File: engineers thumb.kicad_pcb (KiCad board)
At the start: 2 copper layers, 71.1 x 63.5 mm, 53 parts, among them J1 INPUT, J2 9V, J3 GND, J4 Out, J5 GND, J6 LED+, Q1 Q_PMOS_GSD, Q2 BC327, SW1 TREBLE_BOOST, U1 TL072, U2 TL072, U3 LM13700

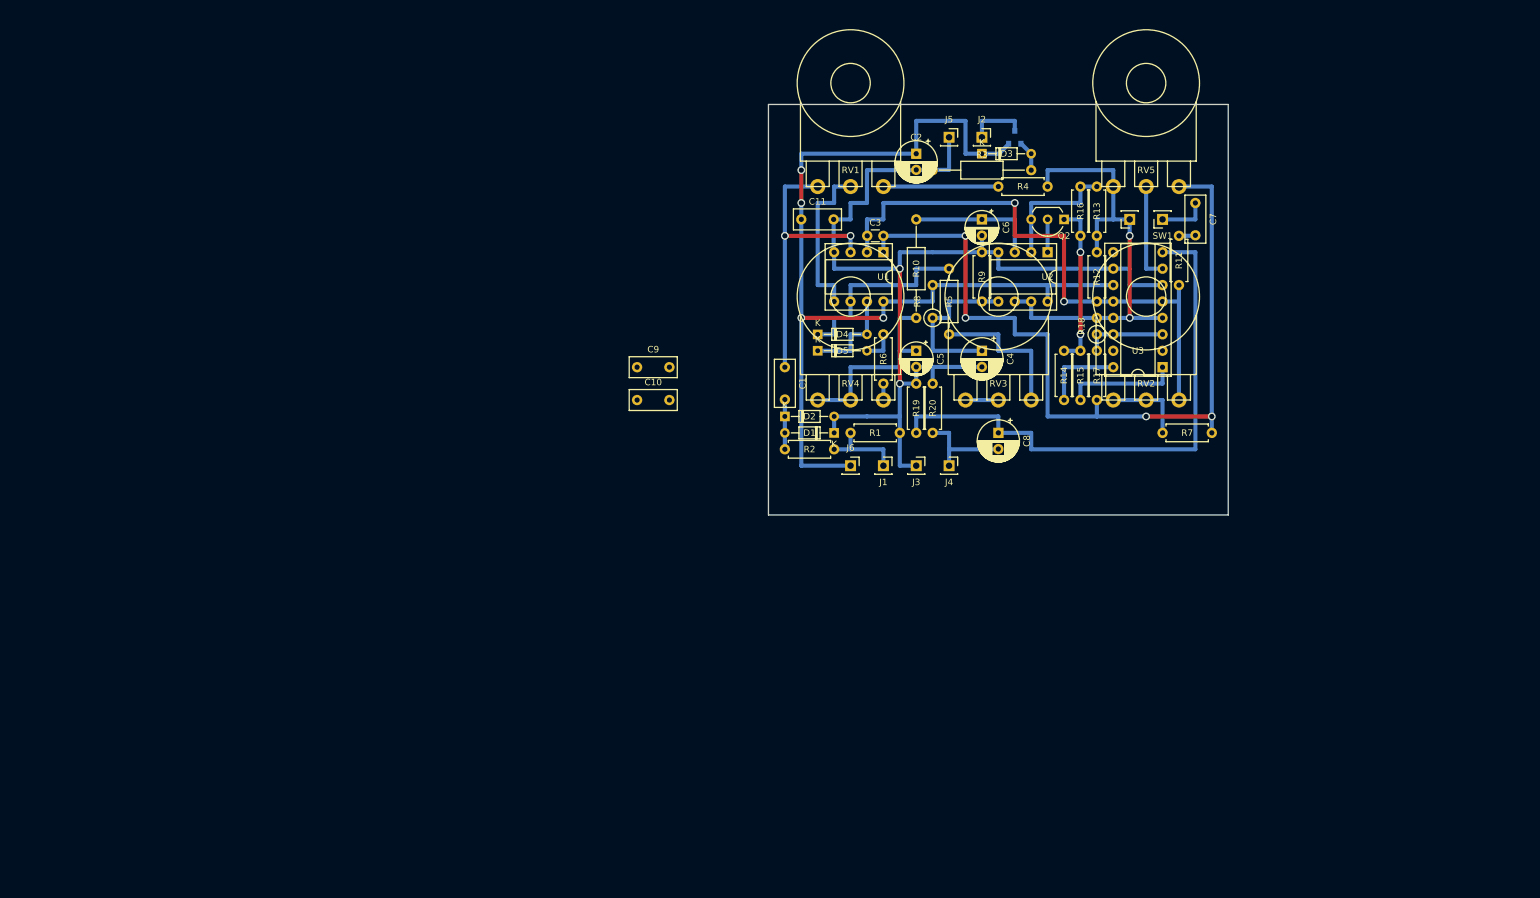
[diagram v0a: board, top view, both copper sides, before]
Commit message: Corrected footprints
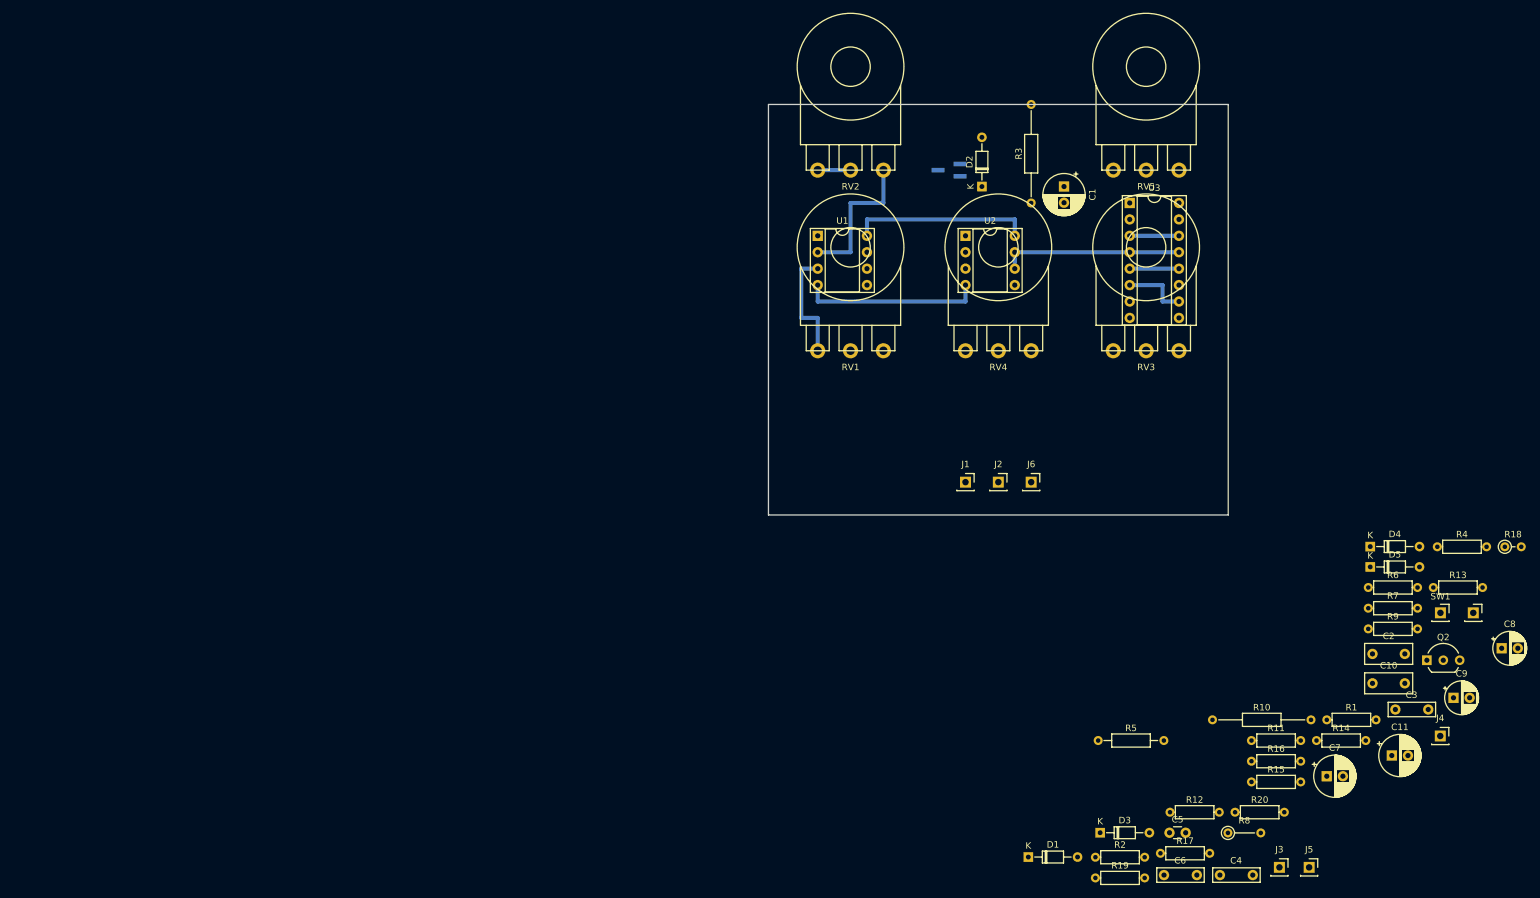
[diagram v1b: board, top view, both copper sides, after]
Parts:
- C1: value 10n -> 47u; footprint Capacitor_THT:C_Rect_L7.2mm_W3.0mm_P5.00mm_FKS2_FKP2_MKS2_MKP2 -> Capacitor_THT:CP_Radial_D6.3mm_P2.50mm
- C10: value 100n -> 4.7n-10n
- C11: value 100n -> 10u; footprint Capacitor_THT:C_Rect_L7.2mm_W3.0mm_P5.00mm_FKS2_FKP2_MKS2_MKP2 -> Capacitor_THT:CP_Radial_D6.3mm_P2.50mm
- C2: value 47u -> 10n; footprint Capacitor_THT:CP_Radial_D6.3mm_P2.50mm -> Capacitor_THT:C_Rect_L7.2mm_W3.0mm_P5.00mm_FKS2_FKP2_MKS2_MKP2
- C3: value 100p -> 100n; footprint Capacitor_THT:C_Disc_D3.0mm_W1.6mm_P2.50mm -> 2.Breadboard components:C_Box_P5.08mm
- C4: value 10u -> 100n; footprint Capacitor_THT:CP_Radial_D6.3mm_P2.50mm -> 2.Breadboard components:C_Box_P5.08mm
- C5: value 1u-2u2 -> 100p; footprint Capacitor_THT:CP_Radial_D5.0mm_P2.50mm -> Capacitor_THT:C_Disc_D3.0mm_W1.6mm_P2.50mm
- C6: value 1u-2u2 -> 100n; footprint Capacitor_THT:CP_Radial_D5.0mm_P2.50mm -> 2.Breadboard components:C_Box_P5.08mm
- C7: value 4.7n-10n -> 10u; footprint Capacitor_THT:C_Rect_L7.2mm_W3.0mm_P5.00mm_FKS2_FKP2_MKS2_MKP2 -> Capacitor_THT:CP_Radial_D6.3mm_P2.50mm
- C8: value 10u -> 1u-2u2; footprint Capacitor_THT:CP_Radial_D6.3mm_P2.50mm -> Capacitor_THT:CP_Radial_D5.0mm_P2.50mm
- C9: value 100n -> 1u-2u2; footprint Capacitor_THT:C_Rect_L7.2mm_W3.0mm_P5.00mm_FKS2_FKP2_MKS2_MKP2 -> Capacitor_THT:CP_Radial_D5.0mm_P2.50mm
- D2: value LED -> 10V Zener
- D3: value 10V Zener -> LED
- J2: value 9V -> GND
- J3: value GND -> 9V
- J4: value Out -> GND
- J5: value GND -> LED+
- J6: value LED+ -> Out
- Q1: footprint Package_TO_SOT_SMD:SOT-23 -> Package_TO_SOT_SMD:SOT-23W_Handsoldering
- R1, R11, R12, R13, R14, R15, R16, R17, R19, R2, R20, R4, R6, R7, R9: footprint Resistor_THT:R_Axial_DIN0207_L6.3mm_D2.5mm_P7.62mm_Horizontal -> 2.Breadboard components:R_Axial_L6mm_D2mm_P7.62mm
- R10, R3: footprint Resistor_THT:R_Axial_DIN0207_L6.3mm_D2.5mm_P15.24mm_Horizontal -> 2.Breadboard components:R_Axial_L6mm_D2mm_P15.24mm
- R18: footprint Resistor_THT:R_Axial_DIN0207_L6.3mm_D2.5mm_P2.54mm_Vertical -> 2.Breadboard components:R_Axial_L6mm_D2mm_P2.54mm
- R5: footprint Resistor_THT:R_Axial_DIN0207_L6.3mm_D2.5mm_P10.16mm_Horizontal -> 2.Breadboard components:R_Axial_L6mm_D2mm_P10.16mm
- R8: footprint Resistor_THT:R_Axial_DIN0207_L6.3mm_D2.5mm_P5.08mm_Vertical -> 2.Breadboard components:R_Axial_L6mm_D2mm_P5.08mm
- U1, U2: footprint Package_DIP:DIP-8_W7.62mm_Socket -> 2.Breadboard components:DIP-8_Socket
- U3: footprint Package_DIP:DIP-16_W7.62mm_Socket -> 2.Breadboard components:DIP-16_Socket
- moved C9 136.2 mm to (273.6, 140.0)
- moved J5 125.9 mm to (251.3, 166.3)
- moved C11 123.4 mm to (264.1, 149.0)
- moved C10 121.9 mm to (261.1, 137.8)
- moved C3 109.7 mm to (264.6, 141.8)
- moved D3 106.6 mm to (218.9, 160.9)
- moved C6 105.3 mm to (228.8, 167.5), turned to 0 degrees
- moved C2 104.7 mm to (261.1, 133.2), turned to 0 degrees
- moved R8 91.8 mm to (238.7, 160.9), turned to 0 degrees
- moved D5 91.8 mm to (260.7, 119.8)
- moved D4 91.6 mm to (260.7, 116.7)
- moved C7 91.0 mm to (254.0, 152.2), turned to 0 degrees
- moved C4 89.1 mm to (237.5, 167.5), turned to 0 degrees
- moved Q2 88.3 mm to (269.5, 134.2), turned to 0 degrees
- moved R4 87.8 mm to (271.1, 116.7)
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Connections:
- C1 pad 1: Net-(C1-Pad1) -> +9V
- C1 pad 2: Net-(C1-Pad2) -> GND
- C10 pad 1: +9V -> Net-(C10-Pad1)
- C10 pad 2: GND -> Net-(C10-Pad2)
- C11 pad 1: +9V -> Net-(C11-Pad1)
- C11 pad 2: GND -> Net-(C11-Pad2)
- C2 pad 1: +9V -> Net-(C2-Pad1)
- C2 pad 2: GND -> Net-(C2-Pad2)
- C3 pad 1: Net-(C3-Pad1) -> +9V
- C3 pad 2: Net-(C3-Pad2) -> GND
- C4 pad 1: Net-(C4-Pad1) -> +9V
- C5 pad 2: GND -> Net-(C5-Pad2)
- C6 pad 1: Net-(C6-Pad1) -> +9V
- C7 pad 2: Net-(C7-Pad2) -> GND
- C8 pad 2: Net-(C8-Pad2) -> GND
- C9 pad 1: +9V -> Net-(C9-Pad1)
- D1 pad 2: Net-(C1-Pad2) -> Net-(C2-Pad2)
- D2 pad 1: Net-(C1-Pad2) -> +9V
- D2 pad 2: GND -> Net-(D2-Pad2)
- D3 pad 1: +9V -> Net-(C2-Pad2)
- D3 pad 2: Net-(D3-Pad2) -> GND
- J2 pad 1: Net-(J2-Pad1) -> GND
- J3 pad 1: GND -> Net-(J3-Pad1)
- J4 pad 1: Net-(C8-Pad2) -> GND
- J5 pad 1: GND -> +9V
- J6 pad 1: +9V -> Net-(C11-Pad2)
- Q1 pad 1: Net-(D3-Pad2) -> Net-(D2-Pad2)
- Q1 pad 3: Net-(J2-Pad1) -> Net-(J3-Pad1)
- R10 pad 1: Net-(C5-Pad1) -> Net-(C8-Pad1)
- R10 pad 2: Net-(C6-Pad1) -> Net-(C9-Pad1)
- R11 pad 1: Net-(C3-Pad1) -> Net-(C5-Pad1)
- R11 pad 2: Net-(C7-Pad2) -> Net-(C10-Pad2)
- R12 pad 1: Net-(C3-Pad1) -> Net-(C5-Pad1)
- R17 pad 1: Net-(C3-Pad2) -> Net-(C5-Pad2)
- R19 pad 2: Net-(C8-Pad1) -> Net-(C11-Pad1)
- R2 pad 2: Net-(C1-Pad2) -> Net-(C2-Pad2)
- R20 pad 2: Net-(C8-Pad2) -> Net-(C11-Pad2)
- R3 pad 2: Net-(D3-Pad2) -> Net-(D2-Pad2)
- R7 pad 2: Net-(C3-Pad2) -> Net-(C5-Pad2)
- R8 pad 1: Net-(C4-Pad1) -> Net-(C7-Pad1)
- R9 pad 2: Net-(C4-Pad1) -> Net-(C7-Pad1)
- RV1 pad 1: Net-(C1-Pad1) -> Net-(C2-Pad1)
- RV2 pad 3: Net-(C3-Pad1) -> Net-(C5-Pad1)
- RV3 pad 1: Net-(C5-Pad1) -> Net-(C8-Pad1)
- RV3 pad 2: Net-(C5-Pad1) -> Net-(C8-Pad1)
- RV4 pad 1: Net-(C5-Pad1) -> Net-(C8-Pad1)
- RV4 pad 2: Net-(C5-Pad1) -> Net-(C8-Pad1)
- RV5 pad 3: Net-(C3-Pad2) -> Net-(C5-Pad2)
- SW1 pad 1: Net-(C7-Pad1) -> Net-(C10-Pad1)
- U1 pad 1: Net-(C3-Pad2) -> Net-(C5-Pad2)
- U1 pad 2: Net-(C3-Pad1) -> Net-(C5-Pad1)
- U1 pad 3: Net-(C1-Pad1) -> Net-(C2-Pad1)
- U2 pad 3: Net-(C6-Pad1) -> Net-(C9-Pad1)
- U2 pad 5: Net-(C4-Pad1) -> Net-(C7-Pad1)
- U3 pad 12: Net-(C3-Pad1) -> Net-(C5-Pad1)
- U3 pad 5: Net-(C3-Pad1) -> Net-(C5-Pad1)
- U3 pad 8: Net-(C8-Pad1) -> Net-(C11-Pad1)
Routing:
- net Net-(C3-Pad2): track 127.0 -> 0.00 mm, vias 4 -> 0
- net +9V: track 154.9 -> 27.9 mm, vias 4 -> 0
- net GND: track 162.8 -> 38.1 mm, vias 2 -> 0
- net Net-(C3-Pad1): track 88.9 -> 0.00 mm, vias 2 -> 0
- net Net-(C8-Pad1): track 86.4 -> 0.00 mm
- net Net-(C1-Pad1): track 45.7 -> 0.00 mm, vias 2 -> 0
- net +4V5: track 71.1 -> 27.9 mm, vias 2 -> 0
- net Net-(D4-Pad1): track 30.5 -> 0.00 mm
- net Net-(RV1-Pad2): track 25.4 -> 0.00 mm
- net Net-(C4-Pad1): track 25.4 -> 0.00 mm
- net Net-(Q2-Pad1): track 25.4 -> 0.00 mm, vias 2 -> 0
- net Net-(R5-Pad2): track 22.9 -> 0.00 mm
- net Net-(C6-Pad1): track 20.3 -> 0.00 mm
- net Net-(Q2-Pad3): track 20.3 -> 0.00 mm
- net Net-(R4-Pad1): track 17.8 -> 0.00 mm
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
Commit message: updated layout
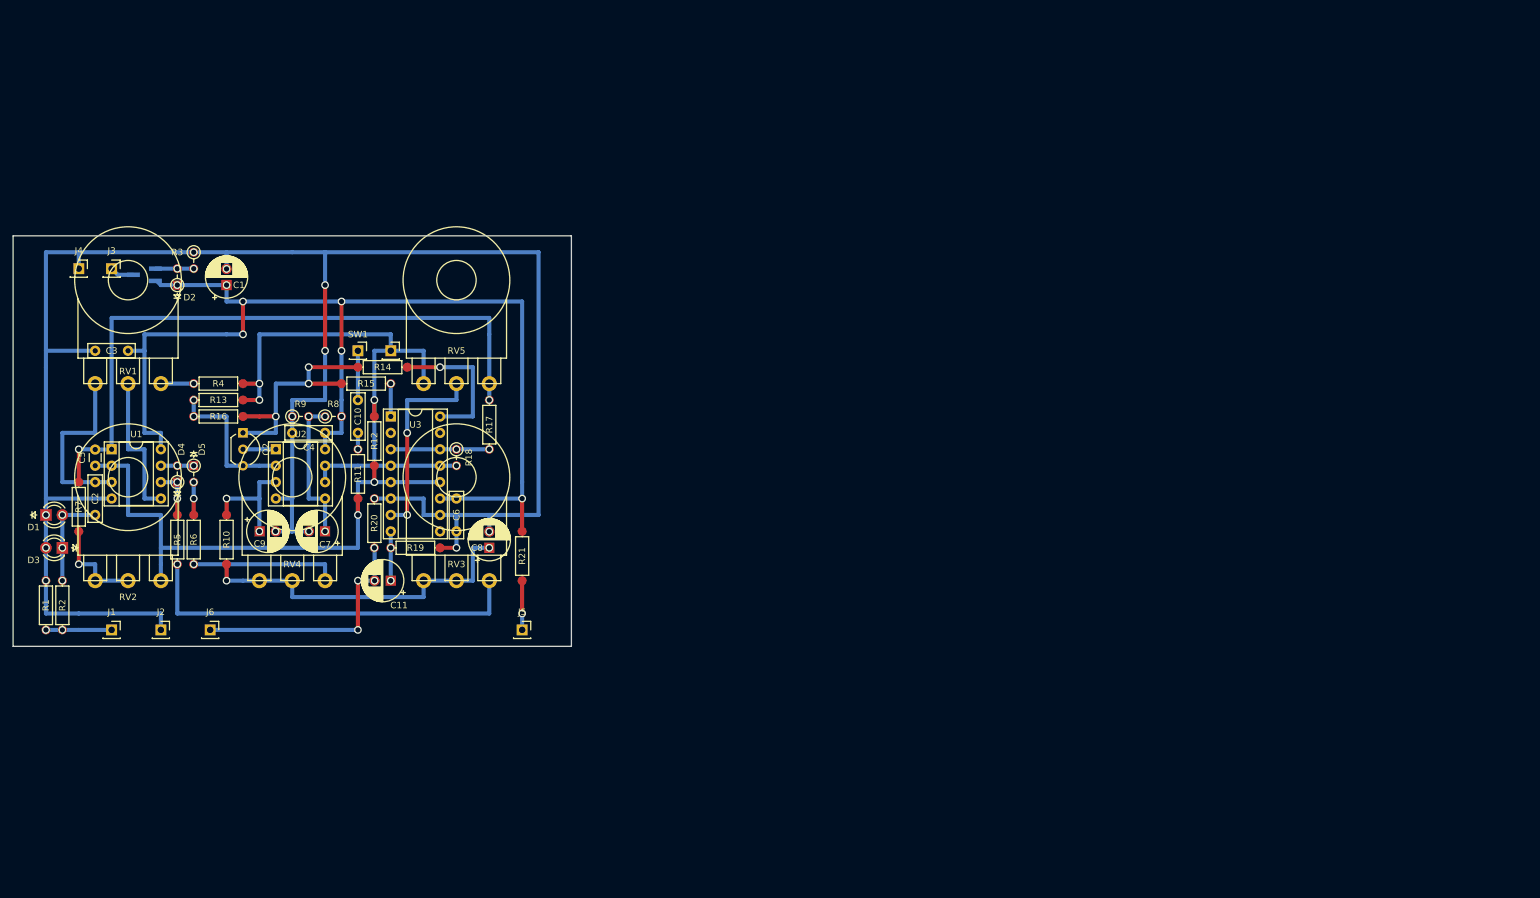
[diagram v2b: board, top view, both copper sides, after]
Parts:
- added R21: R_LED, 2.Breadboard components:R_Axial_Horizontal, F.Cu at (129.5, 121.9)
- C1, C11, C7: footprint Capacitor_THT:CP_Radial_D6.3mm_P2.50mm -> 2.Breadboard components:CP_Vertical
- C10, C2: footprint Capacitor_THT:C_Rect_L7.2mm_W3.0mm_P5.00mm_FKS2_FKP2_MKS2_MKP2 -> 2.Breadboard components:C_Box_P5.08mm
- C5: footprint Capacitor_THT:C_Disc_D3.0mm_W1.6mm_P2.50mm -> 2.Breadboard components:C_Disc_P2.50mm
- C8, C9: footprint Capacitor_THT:CP_Radial_D5.0mm_P2.50mm -> 2.Breadboard components:CP_Vertical
- D1, D3: footprint Diode_THT:D_DO-34_SOD68_P7.62mm_Horizontal -> 2.Breadboard components:LED_D3.0mm_Vertical
- D2, D4, D5: footprint Diode_THT:D_DO-34_SOD68_P7.62mm_Horizontal -> 2.Breadboard components:D_Axial_Vertical
- R1, R11, R12, R13, R14, R15, R16, R17, R19, R2, R20, R4, R6, R7: footprint 2.Breadboard components:R_Axial_L6mm_D2mm_P7.62mm -> 2.Breadboard components:R_Axial_Horizontal
- R10: footprint 2.Breadboard components:R_Axial_L6mm_D2mm_P15.24mm -> 2.Breadboard components:R_Axial_Horizontal
- R18: footprint 2.Breadboard components:R_Axial_L6mm_D2mm_P2.54mm -> 2.Breadboard components:R_Axial_Vertical
- R3: footprint 2.Breadboard components:R_Axial_L6mm_D2mm_P15.24mm -> 2.Breadboard components:R_Axial_Vertical
- R5: footprint 2.Breadboard components:R_Axial_L6mm_D2mm_P10.16mm -> 2.Breadboard components:R_Axial_Horizontal
- R8: footprint 2.Breadboard components:R_Axial_L6mm_D2mm_P5.08mm -> 2.Breadboard components:R_Axial_Vertical
- R9: footprint 2.Breadboard components:R_Axial_L6mm_D2mm_P7.62mm -> 2.Breadboard components:R_Axial_Vertical
- moved J4 222.7 mm to (61.0, 73.7)
- moved C3 203.7 mm to (68.6, 86.4), turned to 180 degrees
- moved J3 203.0 mm to (66.0, 73.7)
- moved R7 199.8 mm to (61.0, 114.3), turned to 90 degrees
- moved C2 199.4 mm to (63.5, 106.7), turned to 270 degrees
- moved R1 198.6 mm to (55.9, 129.5), turned to 90 degrees
- moved R4 194.0 mm to (78.7, 91.4)
- moved R13 193.9 mm to (78.7, 94.0)
- moved Q2 186.5 mm to (86.4, 99.1), turned to 270 degrees
- moved C9 186.4 mm to (88.9, 114.3)
- moved D4 184.8 mm to (76.2, 106.7), turned to 90 degrees
- moved D5 182.7 mm to (78.7, 104.1), turned to 270 degrees
- moved R6 182.0 mm to (78.7, 111.8), turned to 270 degrees
- moved C5 175.6 mm to (63.5, 104.1), turned to 90 degrees
- moved SW1 172.3 mm to (104.1, 86.4)
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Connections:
- J5 pad 1: +9V -> Net-(J5-Pad1)
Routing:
- net GND: track 38.1 -> 310.1 mm, vias 0 -> 13
- net +9V: track 27.9 -> 176.4 mm, vias 0 -> 8
- net Net-(C5-Pad2): track 0.00 -> 101.6 mm, vias 0 -> 2
- net +4V5: track 27.9 -> 94.0 mm, vias 0 -> 4
- net Net-(R5-Pad2): track 0.00 -> 61.0 mm, vias 0 -> 1
- net Net-(C5-Pad1): track 30.5 -> 86.4 mm, vias 0 -> 2
- net Net-(C8-Pad1): track 0.00 -> 53.3 mm, vias 0 -> 2
- net Net-(C11-Pad2): track 0.00 -> 38.2 mm, vias 0 -> 4
- net Net-(Q2-Pad1): track 0.00 -> 38.1 mm, vias 0 -> 3
- net Net-(RV5-Pad2): track 0.00 -> 30.5 mm, vias 0 -> 2
- net Net-(R6-Pad2): track 0.00 -> 22.9 mm, vias 0 -> 1
- net Net-(C7-Pad1): track 0.00 -> 22.9 mm, vias 0 -> 3
- net Net-(RV1-Pad2): track 0.00 -> 22.9 mm
- net Net-(Q2-Pad3): track 0.00 -> 22.9 mm, vias 0 -> 2
- net Net-(R14-Pad1): track 0.00 -> 22.9 mm, vias 0 -> 1
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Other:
- board size 71.1 x 63.5 mm -> 86.4 x 63.5 mm

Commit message: added capacitor
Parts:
- added C12: 100n, 2.Breadboard components:C_Box_P5.08mm, F.Cu at (88.9, 76.2)
- C1: value 47u -> 100u
- moved R20 35.3 mm to (76.2, 127.0), turned to 0 degrees
- moved C10 13.0 mm to (106.7, 81.3)
- moved R14 13.0 mm to (99.1, 91.4)
- moved SW1 11.4 mm to (114.3, 81.3), turned to 270 degrees
- moved R15 10.5 mm to (99.1, 94.0)
- moved C11 9.16 mm to (104.1, 114.3), turned to 270 degrees
- moved R11 8.03 mm to (106.7, 101.6)
- moved R12 7.18 mm to (101.6, 109.2)
- moved R13 7.18 mm to (83.8, 88.9)
- moved R4 7.18 mm to (83.8, 86.4)
- moved J6 5.08 mm to (86.4, 129.5)
- moved R16 5.08 mm to (86.4, 91.4)
- moved C9 3.62 mm to (86.4, 111.8), turned to 270 degrees
- moved C1 2.54 mm to (83.8, 73.7), turned to 180 degrees
- moved C7 2.54 mm to (96.5, 114.3)
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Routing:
- net Net-(Q2-Pad1): track 38.1 -> 17.8 mm
- net +9V: track 176.4 -> 191.6 mm, vias 8 -> 6
- net Net-(R4-Pad1): track 5.08 -> 15.2 mm
- net Net-(Q2-Pad3): track 22.9 -> 33.0 mm
- net +4V5: track 94.0 -> 83.8 mm
- net Net-(R15-Pad1): track 5.08 -> 12.7 mm
- net GND: track 310.1 -> 317.6 mm
- net Net-(C5-Pad2): track 101.6 -> 106.7 mm
- net Net-(C10-Pad2): track 2.54 -> 7.62 mm
- net Net-(C8-Pad1): track 53.3 -> 58.4 mm
- net Net-(RV5-Pad2): track 30.5 -> 35.6 mm
- net Net-(C11-Pad2): track 38.2 -> 35.6 mm
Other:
- board text added: "+9V"
- board text added: "GND"
- board text added: "IN"
- board text added: "LED+"
- board text added: "OUT"
